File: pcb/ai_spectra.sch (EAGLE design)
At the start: 97 parts, among them IC1 ATMEGA328P-PDIP, J1 1X06, J3 1X02ST, U1 MC7805-HOR, U2 TLC2262

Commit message: adding gerbers
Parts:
- added U$18: AI-LOGOXS, Ai_Miscellany:AI-LOGOXS
- LED1, LED10, LED11, LED12, LED13, LED14, LED15, LED16, LED17, LED18, LED19, LED2, LED20, LED21, LED22, LED23, LED24, LED25, LED26, LED27, LED28, LED29, LED3, LED30, LED31, LED32, LED33, LED34, LED35, LED36, LED37, LED38, LED39, LED4, LED40, LED41, LED42, LED43, LED44, LED45, LED46, LED47, LED48, LED5, LED6, LED7, LED8, LED9: value LED-PL9823-F5 -> LED-PL9823-F8; device Ai_LED:LED-PL9823-F5 -> Ai_LED:LED-PL9823-F8
- renumbered J1 to FTDI, PR1 to LDR2, PR2 to LDR1, S1 to RESET, VR1 to VOLUME

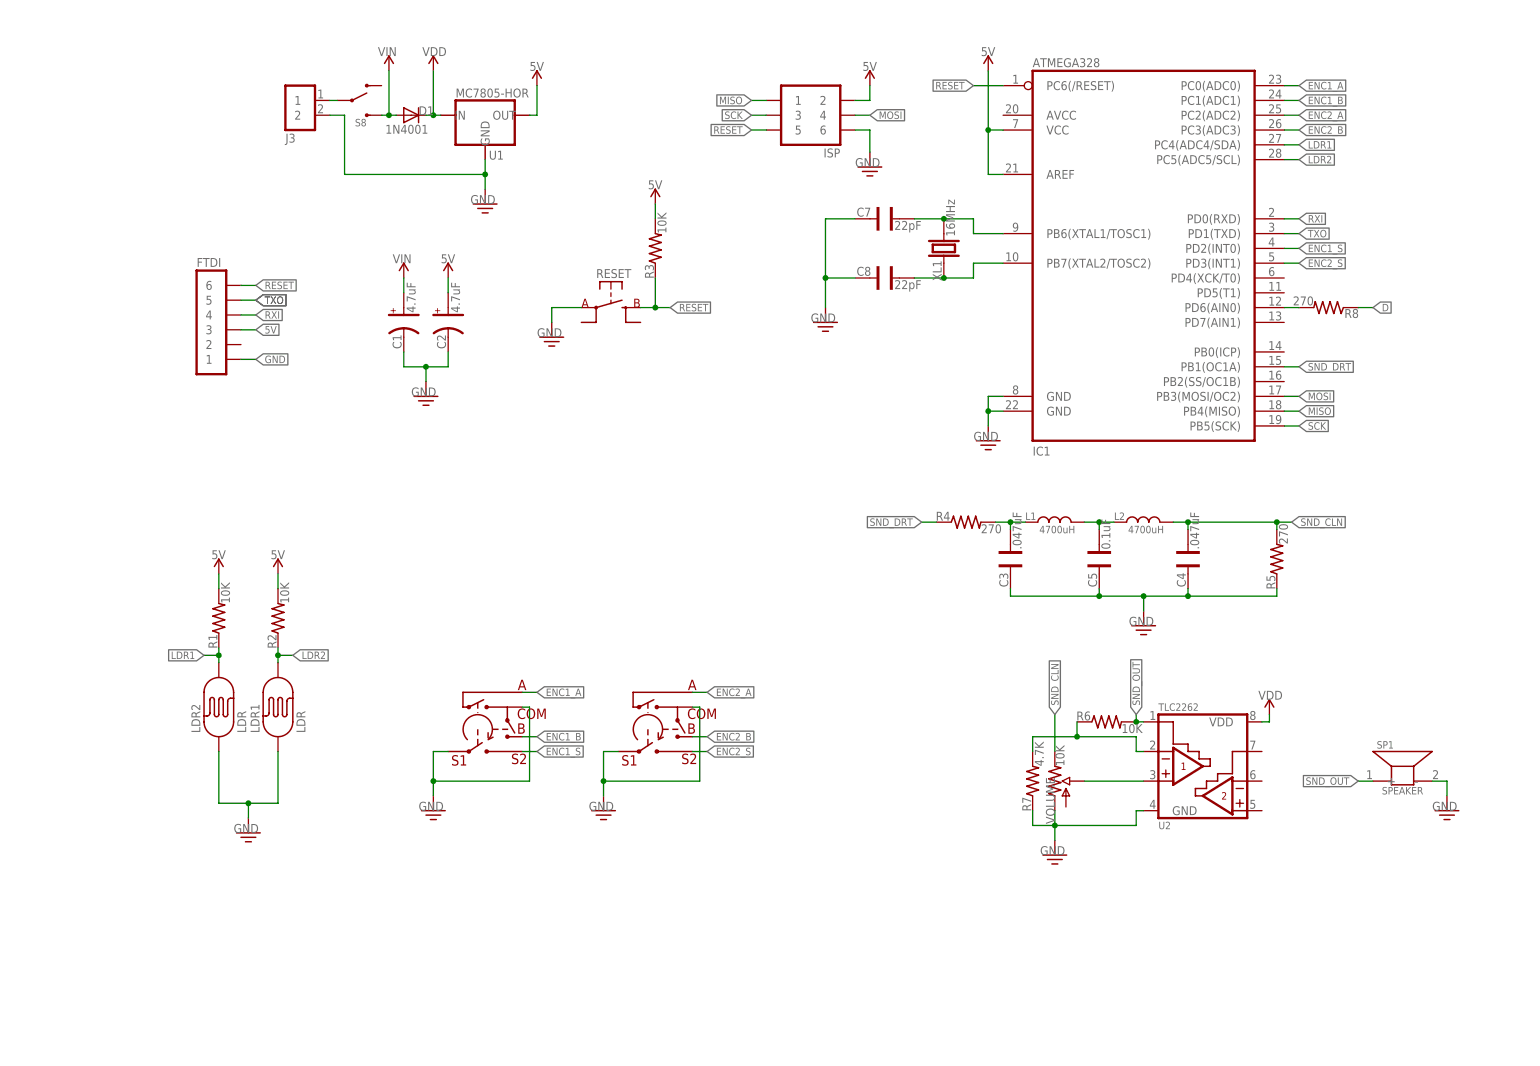
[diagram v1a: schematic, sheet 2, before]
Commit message: updating license, and schematic
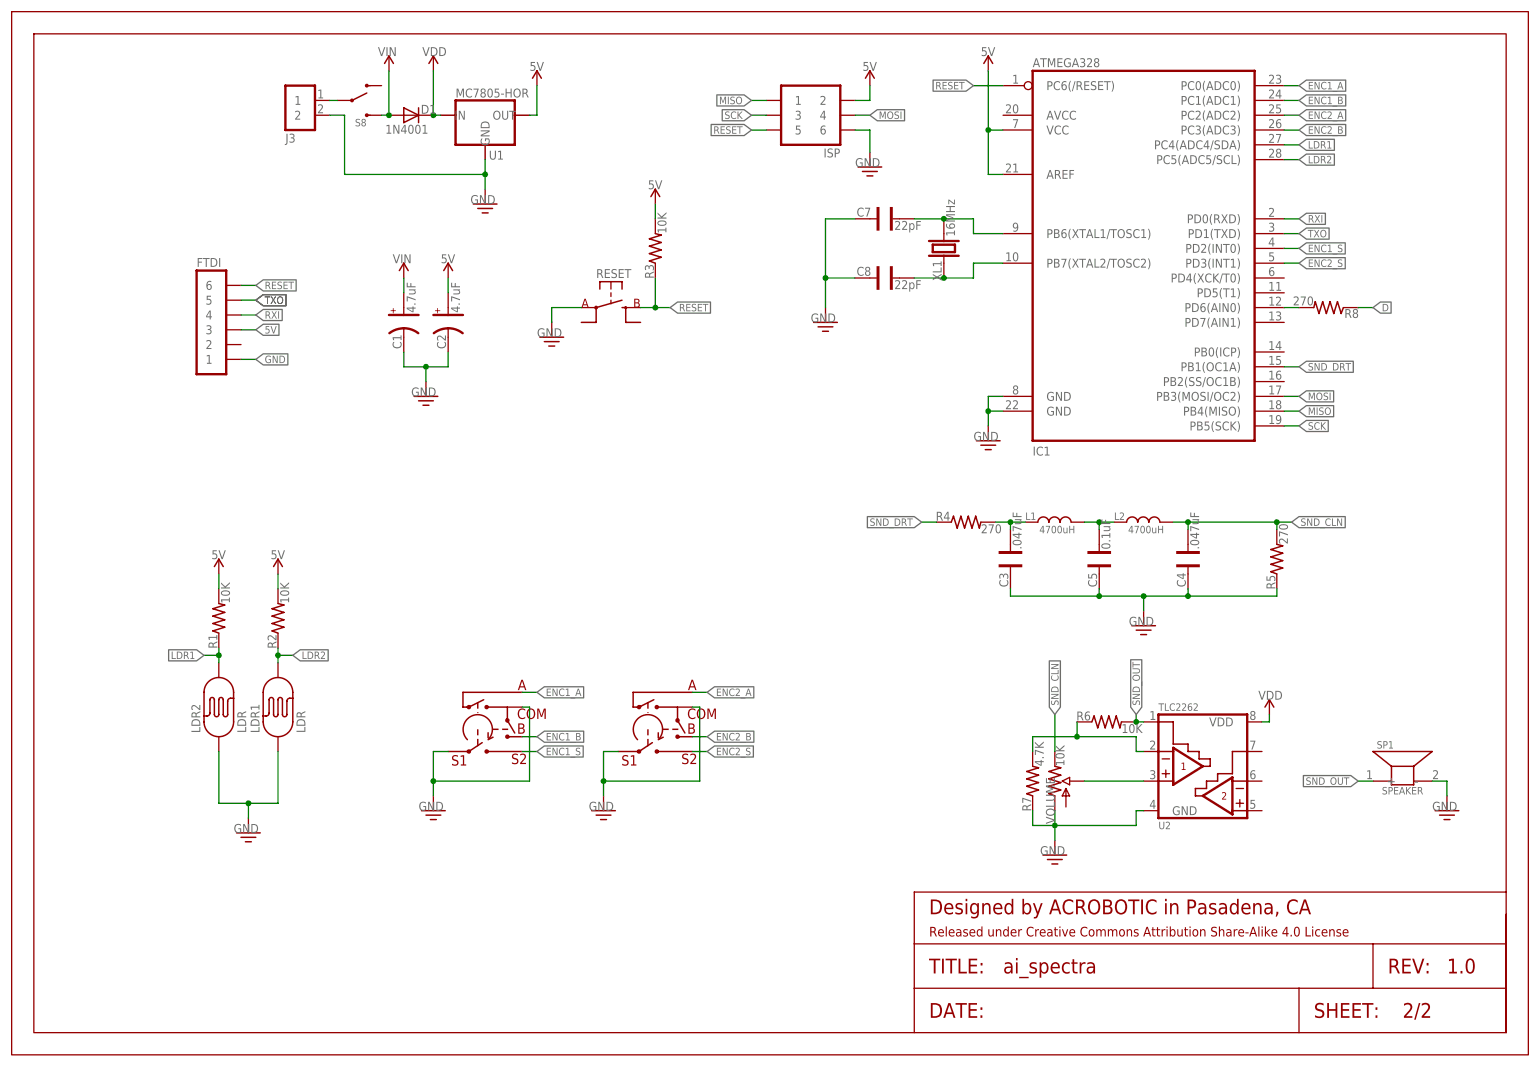
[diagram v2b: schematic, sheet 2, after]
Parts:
- added FRAME1, FRAME2: FRAME-LETTER, Ai_Miscellany:FRAME-LETTER
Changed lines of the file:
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@@
 </classes>
 <parts>
-<part name="FRAME1" library="Ai_Miscellany" deviceset="FRAME-LETTER" device=""/>
+<part name="FRAME1" library="Ai_Miscellany" deviceset="FRAME-LETTER" device="">
+<attribute name="REV" value="1.0"/>
+</part>
 <part name="LED1" library="Ai_LED" deviceset="LED-PL9823" device="-F8" value="LED-PL9823-F8"/>
 <part name="LED2" library="Ai_LED" deviceset="LED-PL9823" device="-F8" value="LED-PL9823-F8"/>
@@
 <part name="STANDOFF4" library="Ai_Electromechanical" deviceset="STAND-OFF" device="4"/>
 <part name="FRAME2" library="Ai_Miscellany" deviceset="FRAME-LETTER" device="">
-<attribute name="AUTHOR" value="A.I. HARDWARE SITHS"/>
 <attribute name="REV" value="1.0"/>
 </part>
@@
 <pinref part="D1" gate="G$1" pin="A"/>
 <wire x1="63.5" y1="161.29" x2="64.77" y2="161.29" width="0.1524" layer="91"/>
-<wire x1="64.77" y1="161.29" x2="66.04" y2="161.29" width="0.1524" layer="91"/>
 <wire x1="64.77" y1="161.29" x2="64.77" y2="168.91" width="0.1524" layer="91"/>
 <junction x="64.77" y="161.29"/>
@@
 <pinref part="D1" gate="G$1" pin="C"/>
 <pinref part="U1" gate="G$1" pin="IN"/>
-<wire x1="71.12" y1="161.29" x2="72.39" y2="161.29" width="0.1524" layer="91"/>
 <wire x1="72.39" y1="161.29" x2="73.66" y2="161.29" width="0.1524" layer="91"/>
 <wire x1="72.39" y1="161.29" x2="72.39" y2="168.91" width="0.1524" layer="91"/>
@@
 </schematic>
 </drawing>
+<compatibility>
+<note version="6.3" minversion="6.2.2" severity="warning">
+Since Version 6.2.2 text objects can contain more than one line,
+which will not be processed correctly with this version.
+</note>
+</compatibility>
 </eagle>

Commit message: updating attribute
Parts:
- FRAME1, FRAME2: REV 1.0 -> 1.1
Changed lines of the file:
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@@
 <parts>
 <part name="FRAME1" library="Ai_Miscellany" deviceset="FRAME-LETTER" device="">
-<attribute name="REV" value="1.0"/>
+<attribute name="REV" value="1.1"/>
 </part>
 <part name="LED1" library="Ai_LED" deviceset="LED-PL9823" device="-F8" value="LED-PL9823-F8"/>
@@
 <part name="STANDOFF4" library="Ai_Electromechanical" deviceset="STAND-OFF" device="4"/>
 <part name="FRAME2" library="Ai_Miscellany" deviceset="FRAME-LETTER" device="">
-<attribute name="REV" value="1.0"/>
+<attribute name="REV" value="1.1"/>
 </part>
 <part name="FTDI" library="Ai_Connectors" deviceset="1X06" device=""/>
